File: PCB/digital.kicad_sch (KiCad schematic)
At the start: 30 parts, among them J14 FINAL_CARRERA_UP, J15 FINAL_CARRERA_DOWN, J3 ICSP, J4 CAN, J6 USART, J7 SPI, J8 RFID_COAX, U2 PIC32MK0256MCJ048-I/Y8X, U3 TCAN334D, Y1 ASZKDV-32.768KHZ-L-T3, Y2 ECS-3225SMV-080-GP-TR

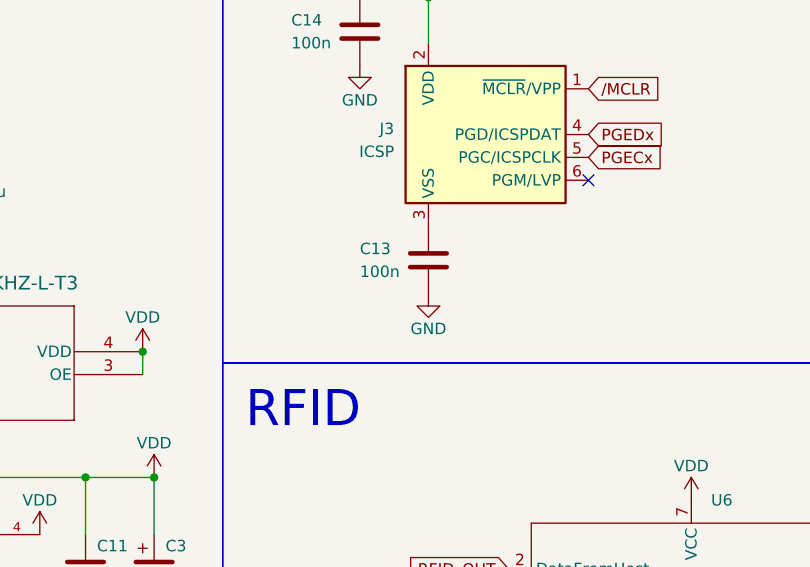
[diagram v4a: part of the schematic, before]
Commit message: correcció missclick capacitat
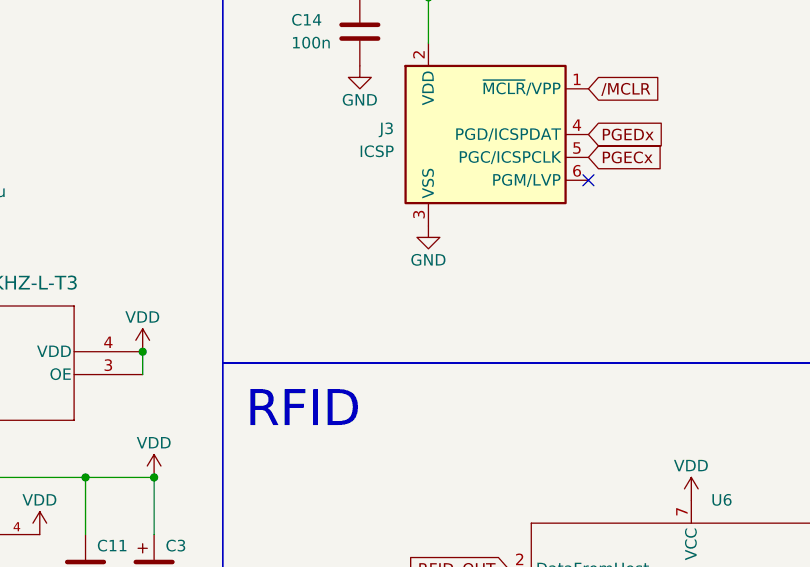
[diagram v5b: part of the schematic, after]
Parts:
- removed C13: 100n, Capacitor_SMD:C_0805_2012Metric, symbol Device:C
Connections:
- net GND: now also J3.3 (VSS)
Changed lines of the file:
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@@
-    )
-  )
-  (symbol (lib_id "Device:C") (at 307.34 58.42 180) (unit 1)
-    (in_bom yes) (on_board yes) (dnp no)
-    (property "Reference" "C13" (at 299.72 57.15 0)
-      (effects (font (size 1.27 1.27)) (justify right))
-    )
-    (property "Value" "100n" (at 299.72 59.69 0)
-      (effects (font (size 1.27 1.27)) (justify right))
-    )
-    (property "Footprint" "Capacitor_SMD:C_0805_2012Metric" (at 306.3748 54.61 0)
-      (effects (font (size 1.27 1.27)) hide)
-    )
-    (property "Datasheet" "~" (at 307.34 58.42 0)
-      (effects (font (size 1.27 1.27)) hide)
-    )
-    (pin "1")
-    (pin "2")
-    (instances
-      (project "DIJOUS_4_PORTES"
-        (path "/69b34976-047e-478e-bd76-9b6ef0dba356/6b83d062-cc2b-4223-9dc9-bddc64623104"
-          (reference "C13") (unit 1)
-        )
-      )
     )
   )
@@
     )
   )
-  (symbol (lib_id "power:GND") (at 307.34 62.23 0) (unit 1)
-    (in_bom yes) (on_board yes) (dnp no)
-    (property "Reference" "#PWR026" (at 307.34 68.58 0)
-      (effects (font (size 1.27 1.27)) hide)
-    )
-    (property "Value" "GND" (at 307.34 66.04 0)
-      (effects (font (size 1.27 1.27)))
-    )
-    (property "Footprint" "" (at 307.34 62.23 0)
-      (effects (font (size 1.27 1.27)) hide)
-    )
-    (property "Datasheet" "" (at 307.34 62.23 0)
-      (effects (font (size 1.27 1.27)) hide)
-    )
+  (symbol (lib_id "power:GND") (at 307.34 54.61 0) (unit 1)
+    (in_bom yes) (on_board yes) (dnp no)
+    (property "Reference" "#PWR026" (at 307.34 60.96 0)
+      (effects (font (size 1.27 1.27)) hide)
+    )
+    (property "Value" "GND" (at 307.34 58.42 0)
+      (effects (font (size 1.27 1.27)))
+    )
+    (property "Footprint" "" (at 307.34 54.61 0)
+      (effects (font (size 1.27 1.27)) hide)
+    )
+    (property "Datasheet" "" (at 307.34 54.61 0)
+      (effects (font (size 1.27 1.27)) hide)
+    )

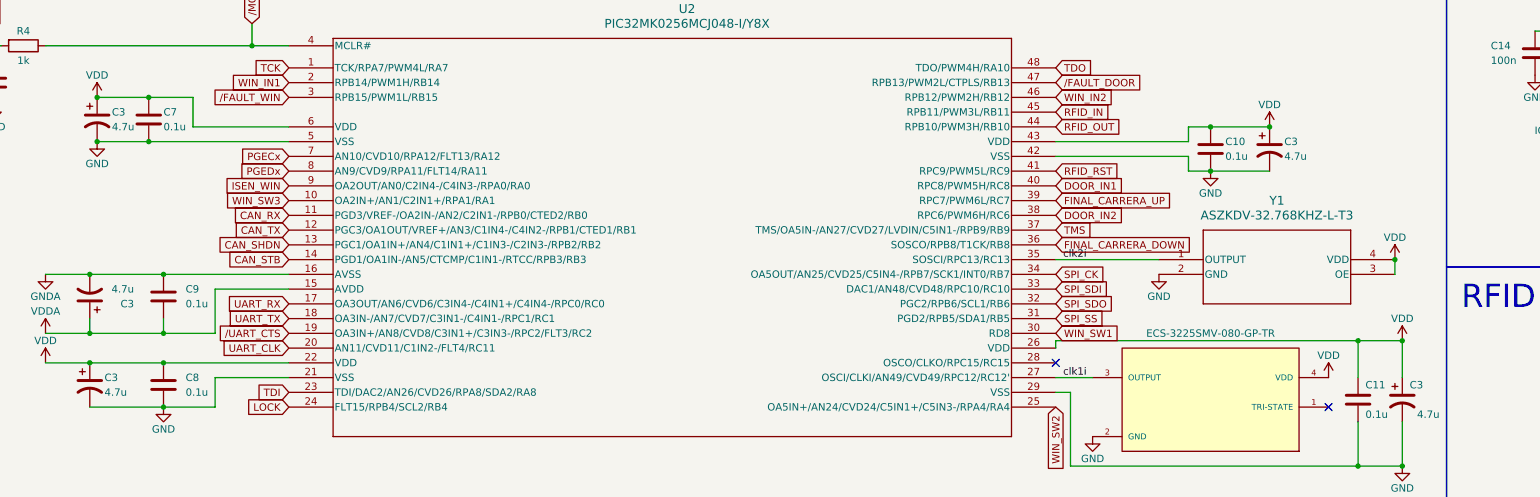
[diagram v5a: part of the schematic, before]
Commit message: netclasses esquematic
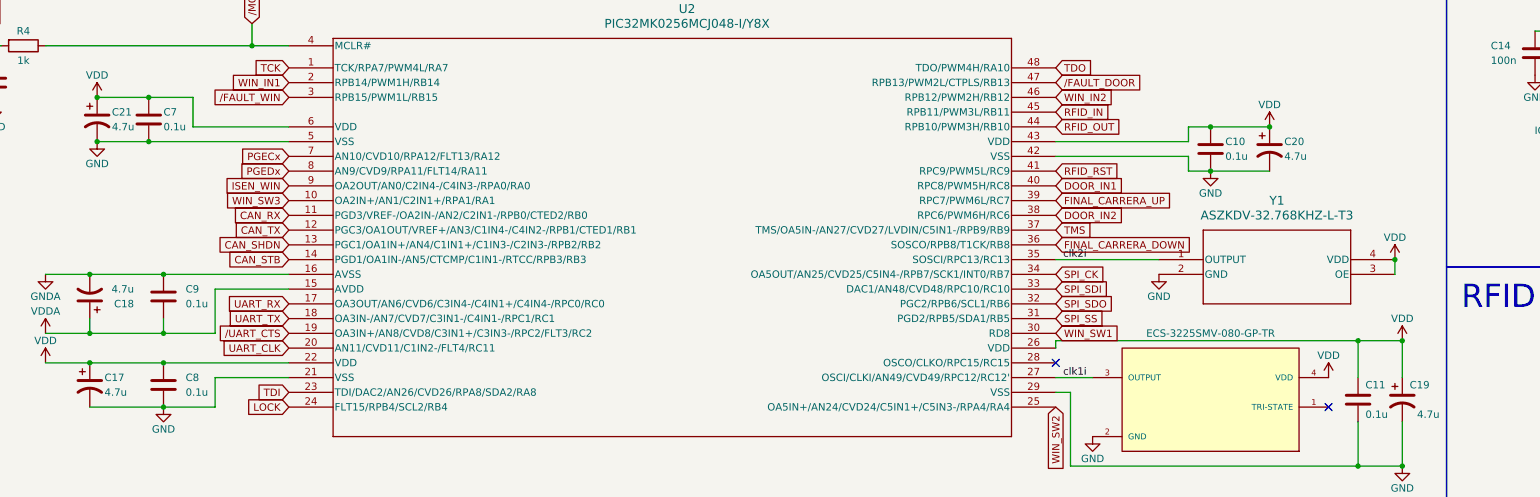
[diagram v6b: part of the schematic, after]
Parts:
- renumbered C3 to C17, C3 to C18, C3 to C19, C3 to C20, C3 to C21
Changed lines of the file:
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@@
   (symbol (lib_id "Device:C_Polarized_US") (at 254 49.53 0) (unit 1)
     (in_bom yes) (on_board yes) (dnp no)
-    (property "Reference" "C3" (at 256.54 48.26 0)
+    (property "Reference" "C20" (at 256.54 48.26 0)
       (effects (font (size 1.27 1.27)) (justify left))
     )
@@
     (instances
       (project "DIJOUS_4_PORTES"
-        (path "/69b34976-047e-478e-bd76-9b6ef0dba356/0e58b9bb-7a32-4563-ae50-f5e325ba8348"
-          (reference "C3") (unit 1)
-        )
         (path "/69b34976-047e-478e-bd76-9b6ef0dba356/6b83d062-cc2b-4223-9dc9-bddc64623104"
           (reference "C20") (unit 1)
@@
   (symbol (lib_id "Device:C_Polarized_US") (at 50.8 74.93 180) (unit 1)
     (in_bom yes) (on_board yes) (dnp no)
-    (property "Reference" "C3" (at 58.42 76.2 0)
+    (property "Reference" "C18" (at 58.42 76.2 0)
       (effects (font (size 1.27 1.27)) (justify left))
     )
@@
     (instances
       (project "DIJOUS_4_PORTES"
-        (path "/69b34976-047e-478e-bd76-9b6ef0dba356/0e58b9bb-7a32-4563-ae50-f5e325ba8348"
-          (reference "C3") (unit 1)
-        )
         (path "/69b34976-047e-478e-bd76-9b6ef0dba356/6b83d062-cc2b-4223-9dc9-bddc64623104"
           (reference "C18") (unit 1)
@@
   (symbol (lib_id "Device:C_Polarized_US") (at 50.8 90.17 0) (unit 1)
     (in_bom yes) (on_board yes) (dnp no)
-    (property "Reference" "C3" (at 53.34 88.9 0)
+    (property "Reference" "C17" (at 53.34 88.9 0)
       (effects (font (size 1.27 1.27)) (justify left))
     )
@@
     (instances
       (project "DIJOUS_4_PORTES"
-        (path "/69b34976-047e-478e-bd76-9b6ef0dba356/0e58b9bb-7a32-4563-ae50-f5e325ba8348"
-          (reference "C3") (unit 1)
-        )
         (path "/69b34976-047e-478e-bd76-9b6ef0dba356/6b83d062-cc2b-4223-9dc9-bddc64623104"
           (reference "C17") (unit 1)
@@
   (symbol (lib_id "Device:C_Polarized_US") (at 276.86 92.71 0) (unit 1)
     (in_bom yes) (on_board yes) (dnp no)
-    (property "Reference" "C3" (at 278.13 90.17 0)
+    (property "Reference" "C19" (at 278.13 90.17 0)
       (effects (font (size 1.27 1.27)) (justify left))
     )
@@
     (instances
       (project "DIJOUS_4_PORTES"
-        (path "/69b34976-047e-478e-bd76-9b6ef0dba356/0e58b9bb-7a32-4563-ae50-f5e325ba8348"
-          (reference "C3") (unit 1)
-        )
         (path "/69b34976-047e-478e-bd76-9b6ef0dba356/6b83d062-cc2b-4223-9dc9-bddc64623104"
           (reference "C19") (unit 1)
@@
   (symbol (lib_id "Device:C_Polarized_US") (at 52.07 44.45 0) (unit 1)
     (in_bom yes) (on_board yes) (dnp no)
-    (property "Reference" "C3" (at 54.61 43.18 0)
+    (property "Reference" "C21" (at 54.61 43.18 0)
       (effects (font (size 1.27 1.27)) (justify left))
     )
@@
     (instances
       (project "DIJOUS_4_PORTES"
-        (path "/69b34976-047e-478e-bd76-9b6ef0dba356/0e58b9bb-7a32-4563-ae50-f5e325ba8348"
-          (reference "C3") (unit 1)
-        )
         (path "/69b34976-047e-478e-bd76-9b6ef0dba356/6b83d062-cc2b-4223-9dc9-bddc64623104"
           (reference "C21") (unit 1)

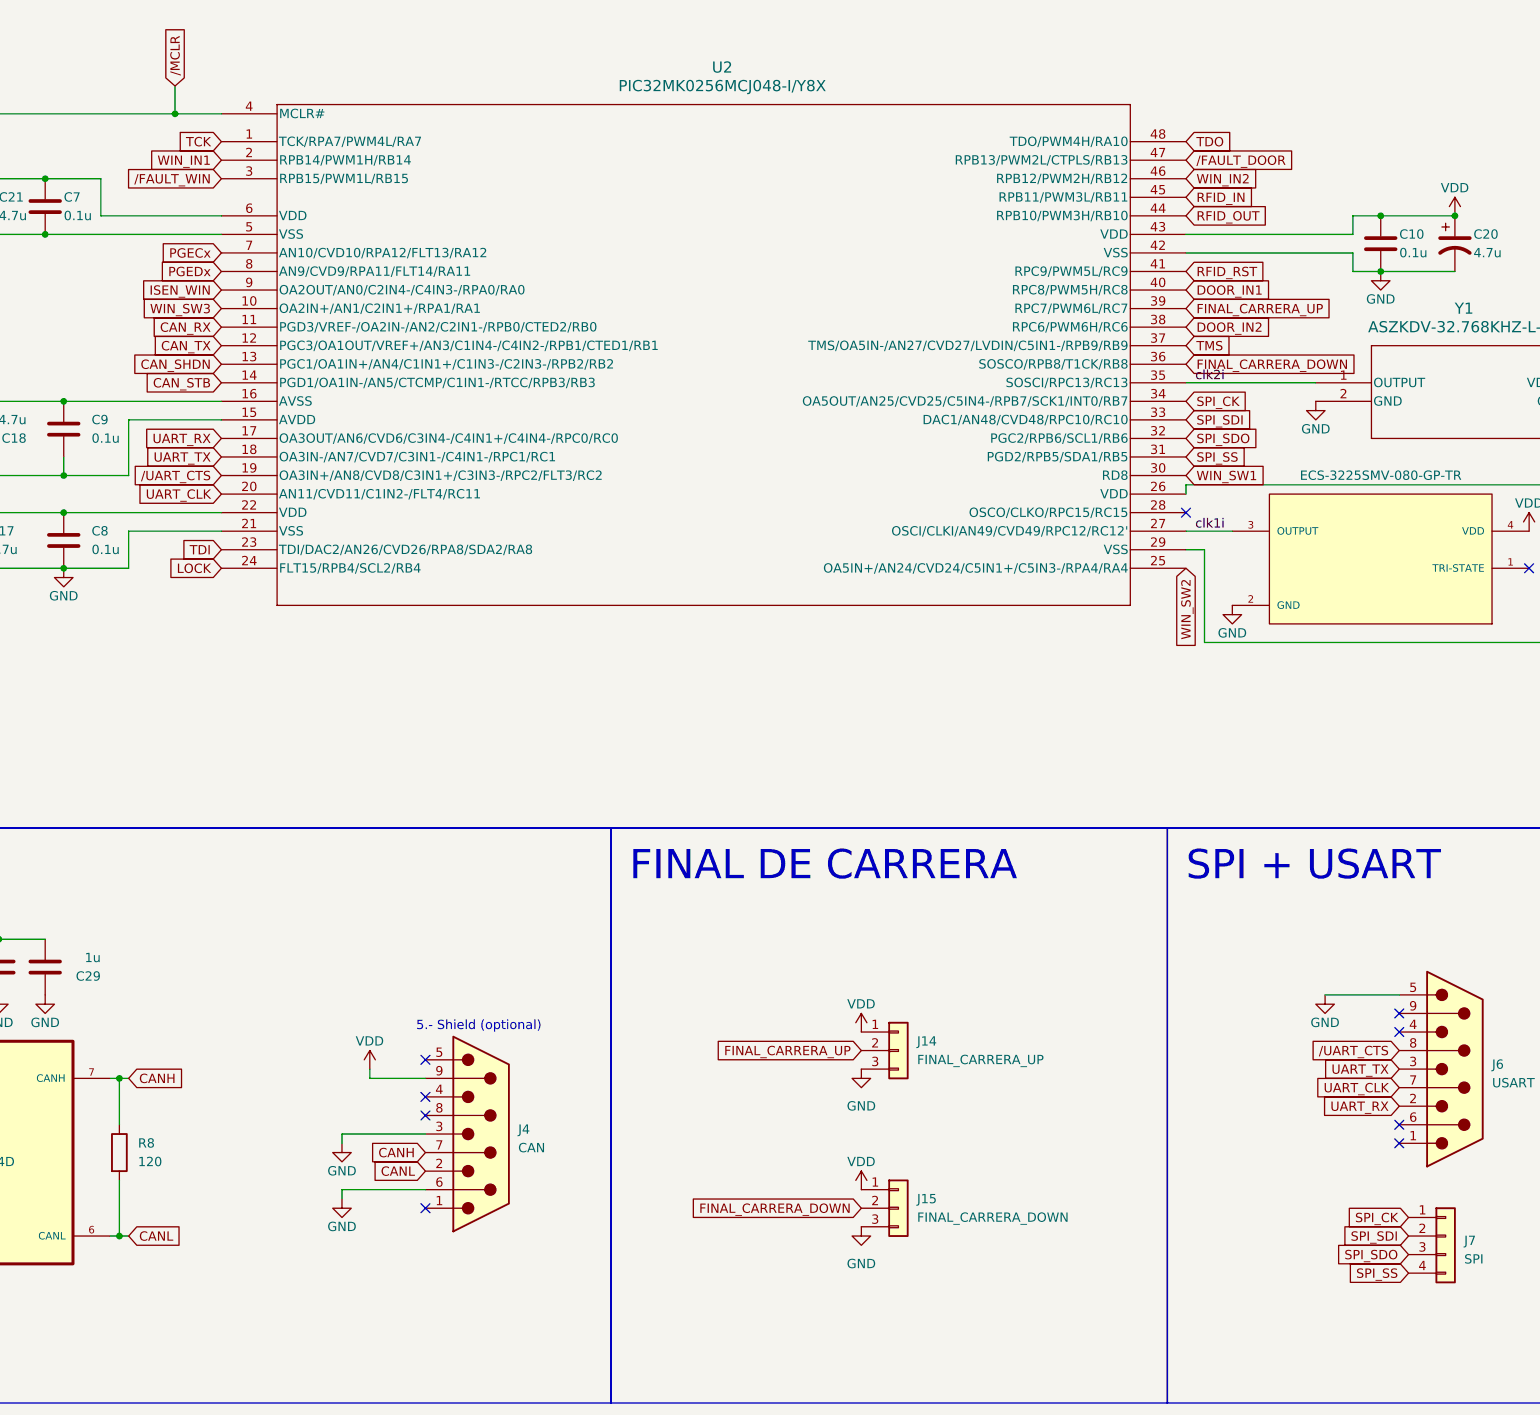
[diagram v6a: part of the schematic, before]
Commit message: first PCB done, need to correct vias and solve all DRC errors
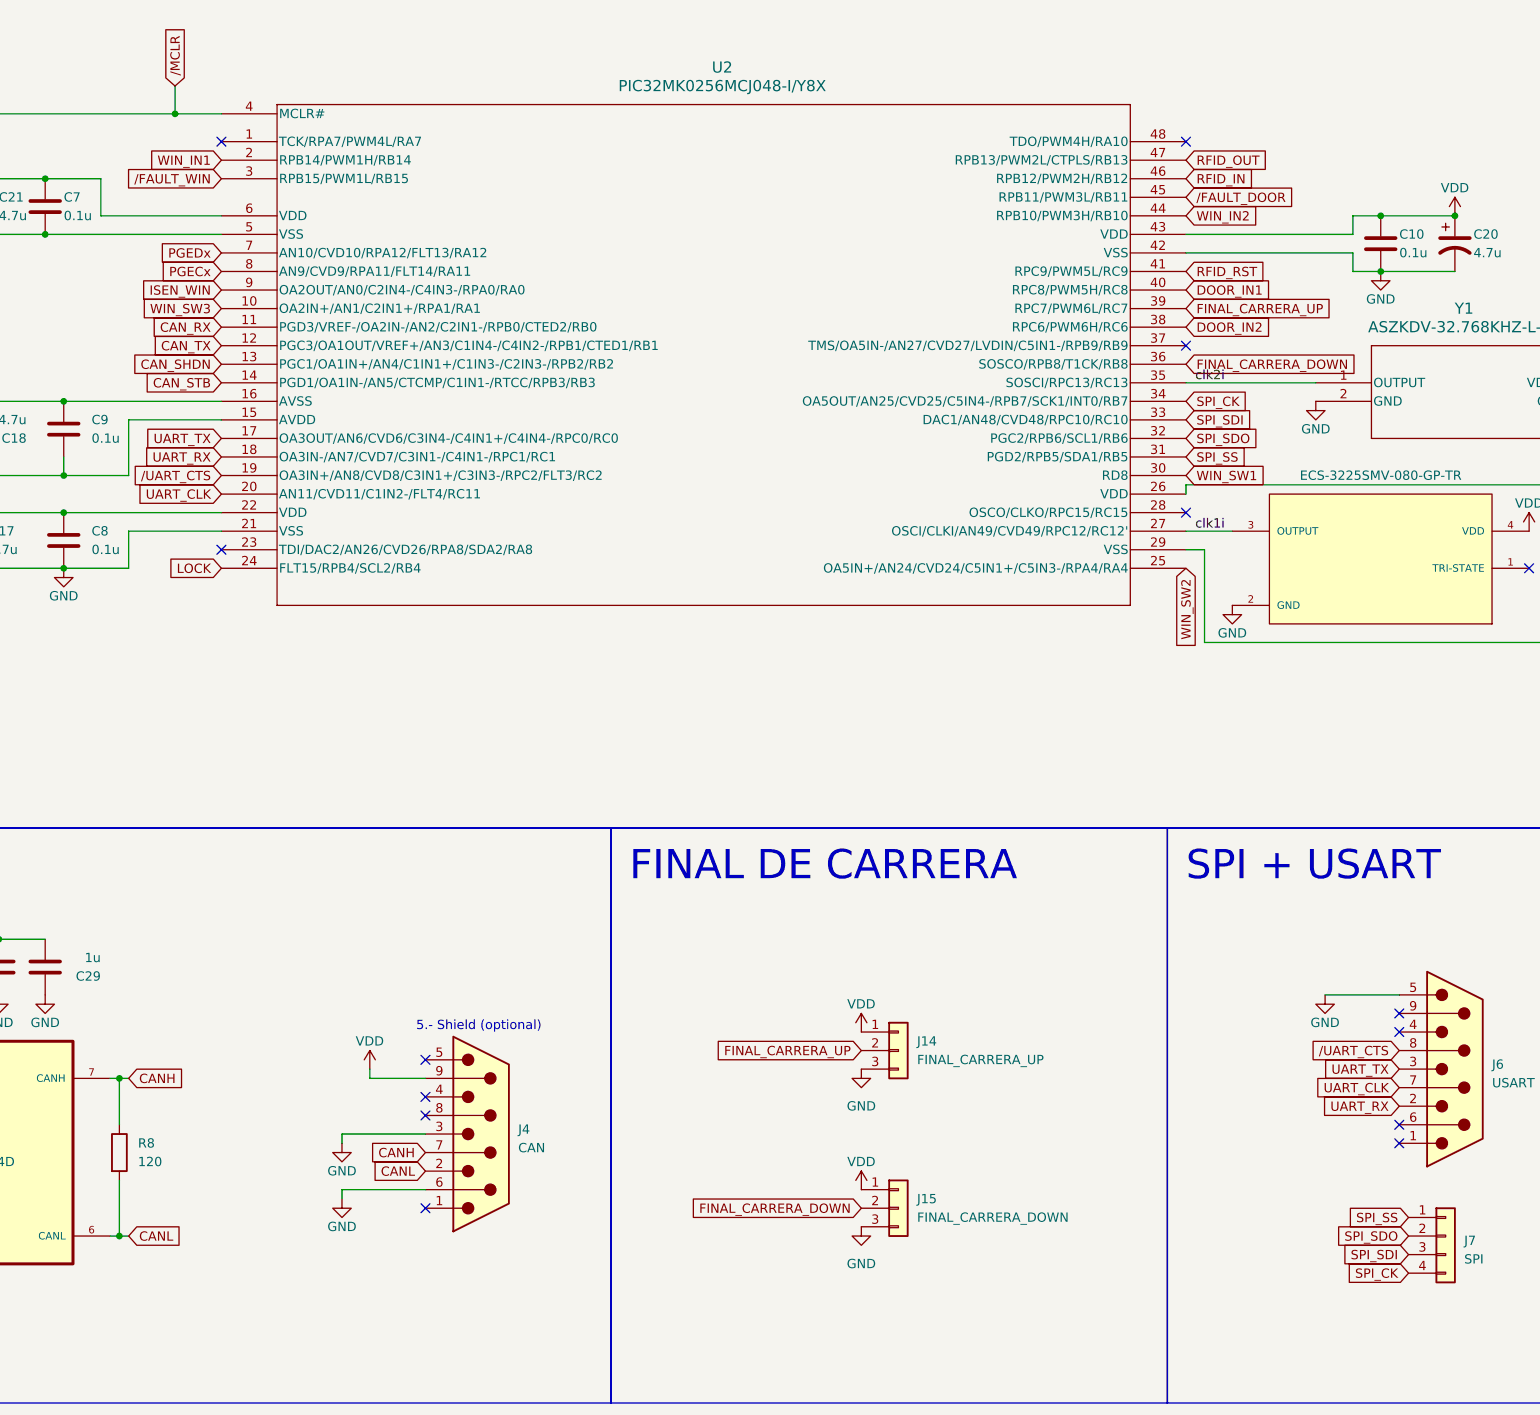
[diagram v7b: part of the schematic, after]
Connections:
- net PGECx: now also U2.8 (AN9/CVD9/RPA11/FLT14/RA11); no longer U2.7 (AN10/CVD10/RPA12/FLT13/RA12)
- net PGEDx: now also U2.7 (AN10/CVD10/RPA12/FLT13/RA12); no longer U2.8 (AN9/CVD9/RPA11/FLT14/RA11)
- net RFID_IN: now also U2.46 (RPB12/PWM2H/RB12); no longer U2.45 (RPB11/PWM3L/RB11)
- net RFID_OUT: now also U2.47 (RPB13/PWM2L/CTPLS/RB13); no longer U2.44 (RPB10/PWM3H/RB10)
- net SPI_CK: now also J7.4 (Pin_4); no longer J7.1 (Pin_1)
- net SPI_SDI: now also J7.3 (Pin_3); no longer J7.2 (Pin_2)
- net SPI_SDO: now also J7.2 (Pin_2); no longer J7.3 (Pin_3)
- net SPI_SS: now also J7.1 (Pin_1); no longer J7.4 (Pin_4)
- net UART_RX: now also U2.18 (OA3IN-/AN7/CVD7/C3IN1-/C4IN1-/RPC1/RC1); no longer U2.17 (OA3OUT/AN6/CVD6/C3IN4-/C4IN1+/C4IN4-/RPC0/RC0)
- net UART_TX: now also U2.17 (OA3OUT/AN6/CVD6/C3IN4-/C4IN1+/C4IN4-/RPC0/RC0); no longer U2.18 (OA3IN-/AN7/CVD7/C3IN1-/C4IN1-/RPC1/RC1)
- net WIN_IN2: now also U2.44 (RPB10/PWM3H/RB10); no longer U2.46 (RPB12/PWM2H/RB12)
- net /FAULT_DOOR: now also U2.45 (RPB11/PWM3L/RB11); no longer U2.47 (RPB13/PWM2L/CTPLS/RB13)
- net TCK: no longer names the net of U2.1 (TCK/RPA7/PWM4L/RA7)
- net TDI: no longer names the net of U2.23 (TDI/DAC2/AN26/CVD26/RPA8/SDA2/RA8)
- net TDO: no longer names the net of U2.48 (TDO/PWM4H/RA10)
- net TMS: no longer names the net of U2.37 (TMS/OA5IN-/AN27/CVD27/LVDIN/C5IN1-/RPB9/RB9)
- no-connect marks 15 -> 19
